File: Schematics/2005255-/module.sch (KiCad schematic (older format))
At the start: 0 parts

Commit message: Finished first complete pass at 2005255- CAD drawings.
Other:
- note added: "2005255"
- note added: "4 BIT MODULE"
- note added: "80230"
- note added: "LOGIC FLOW DIAGRAM"
- note added: "MODULE NO.A8"
- note added: "____"
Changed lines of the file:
@@
 	20700 17550 22900 17550
 $Comp
-L AGC_DSKY:PWR_FLAG #FLG?
+L AGC_DSKY:PWR_FLAG #FLG0103
 U 1 1 61A08F95
 P 22900 17550
-F 0 "#FLG?" H 22900 18075 50  0001 C CNN
+F 0 "#FLG0103" H 22900 18075 50  0001 C CNN
 F 1 "PWR_FLAG" H 22910 18010 50  0001 C CNN
 F 2 "" H 22900 17550 50  0001 C CNN
@@
 	22900 17550 25125 17550
 $Comp
-L AGC_DSKY:PWR_FLAG #FLG?
+L AGC_DSKY:PWR_FLAG #FLG0102
 U 1 1 61A08FB9
 P 22900 16425
-F 0 "#FLG?" H 22900 16950 50  0001 C CNN
+F 0 "#FLG0102" H 22900 16950 50  0001 C CNN
 F 1 "PWR_FLAG" H 22910 16885 50  0001 C CNN
 F 2 "" H 22900 16425 50  0001 C CNN
@@
 	22900 16425 25125 16425
 $Comp
-L AGC_DSKY:PWR_FLAG #FLG?
+L AGC_DSKY:PWR_FLAG #FLG0101
 U 1 1 61A08FDD
 P 22900 15375
-F 0 "#FLG?" H 22900 15900 50  0001 C CNN
+F 0 "#FLG0101" H 22900 15900 50  0001 C CNN
 F 1 "PWR_FLAG" H 22910 15835 50  0001 C CNN
 F 2 "" H 22900 15375 50  0001 C CNN
@@
 Wire Wire Line
 	22900 15375 25125 15375
+Text Notes 38925 31800 0    250  ~ 50
+LOGIC FLOW DIAGRAM
+Text Notes 40875 33100 0    250  ~ 50
+2005255
+Text Notes 38250 33100 0    250  ~ 50
+80230
+Text Notes 39275 32150 0    200  ~ 40
+MODULE NO.A8
+Text Notes 39950 32450 0    200  ~ 40
+4 BIT MODULE
+Text Notes 38900 33375 0    140  ~ 28
+____
+Connection ~ 27250 17025
 $EndSCHEMATC

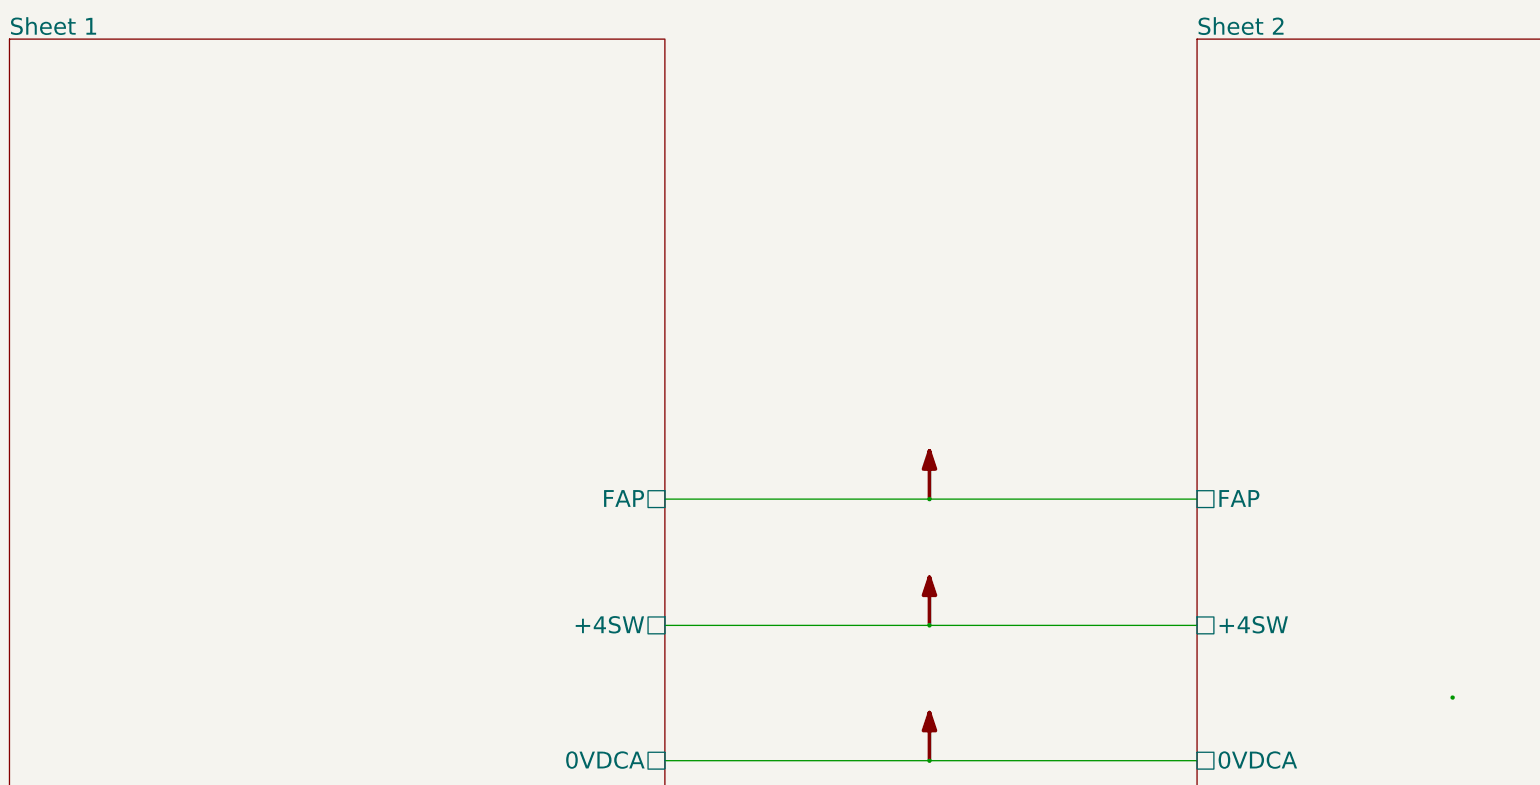
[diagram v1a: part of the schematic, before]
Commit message: Cross-checked/corrected connector-pad labels for module A8 CAD, vs Mike's pin database.
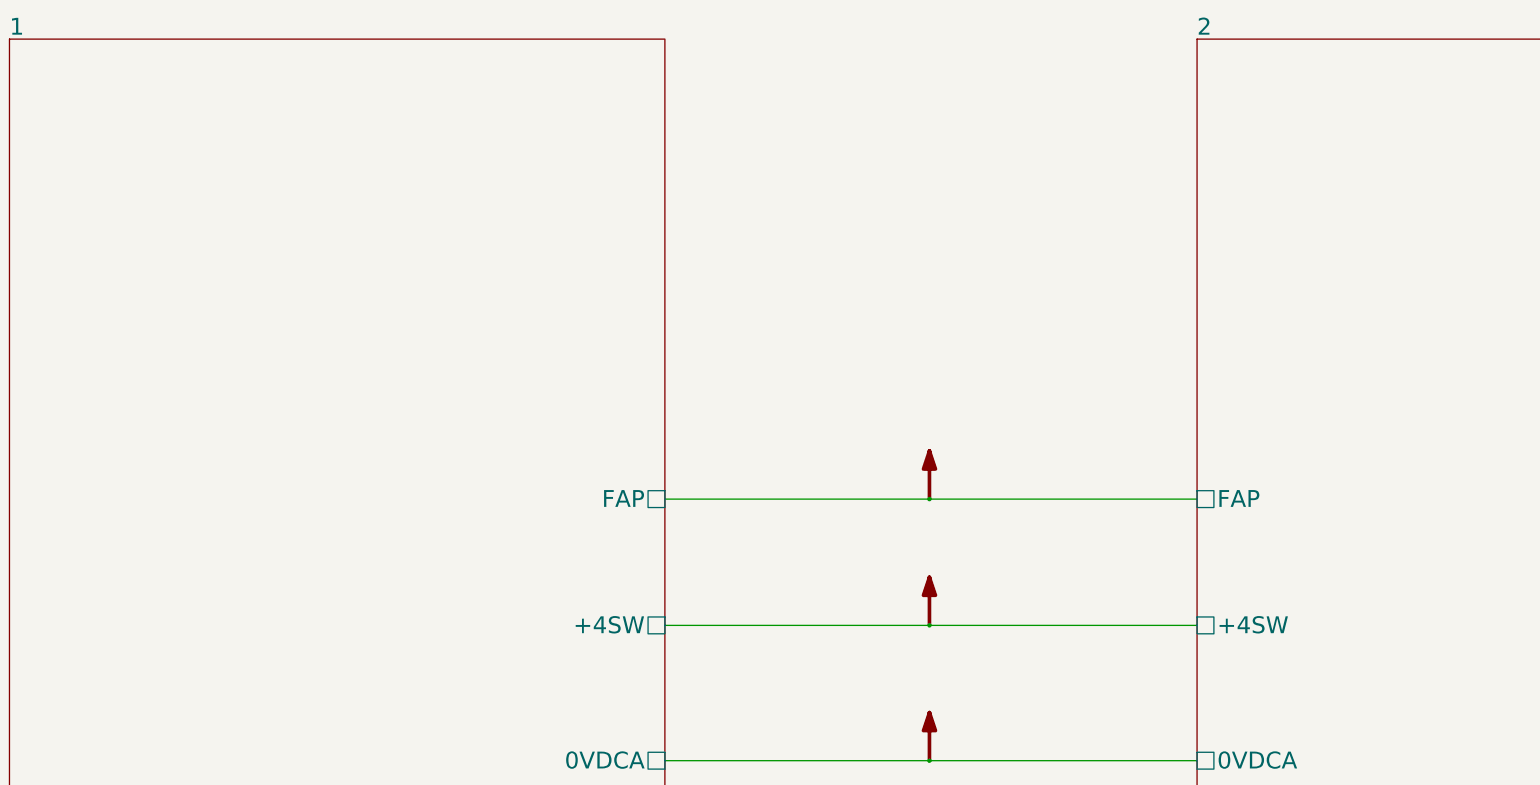
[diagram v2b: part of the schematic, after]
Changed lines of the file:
@@
 S 15250 11550 5450 8975
 U 5B8E7731
-F0 "Sheet 1" 140
+F0 "1" 140
 F1 "2005255--p1of2.sch" 140
 F2 "0VDCA" U R 20700 17550 140
@@
 S 25125 11550 5450 8975
 U 5B8E7796
-F0 "Sheet 2" 140
+F0 "2" 140
 F1 "2005255--p2of2.sch" 140
 F2 "0VDCA" U L 25125 17550 140
@@
 Text Notes 38900 33375 0    140  ~ 28
 ____
-Connection ~ 27250 17025
 $EndSCHEMATC
